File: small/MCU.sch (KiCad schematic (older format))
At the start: 27 parts, among them IC1 PIC32MX350F256H-V_PT, J3 Micro_SD_Card, J4 Conn_01x05_Female, U5 AT25M02, U8 PCF8563T, Y2 Crystal

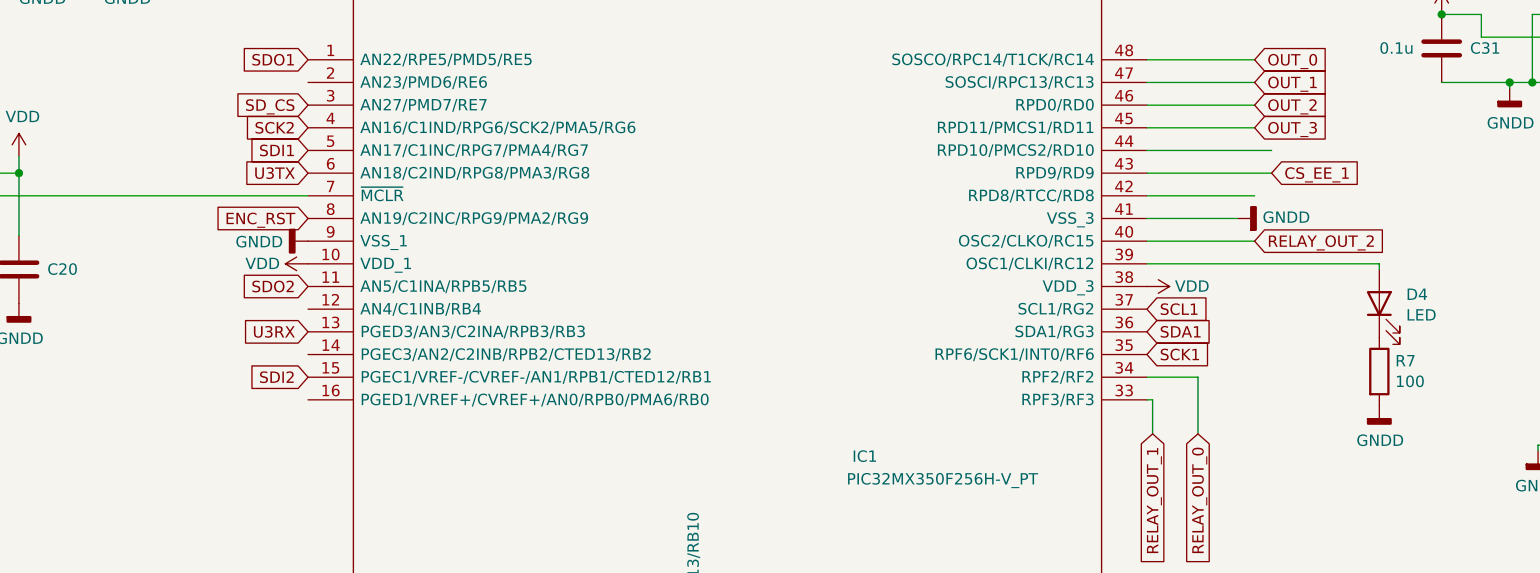
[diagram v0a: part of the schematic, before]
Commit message: sim800 changed to sim808
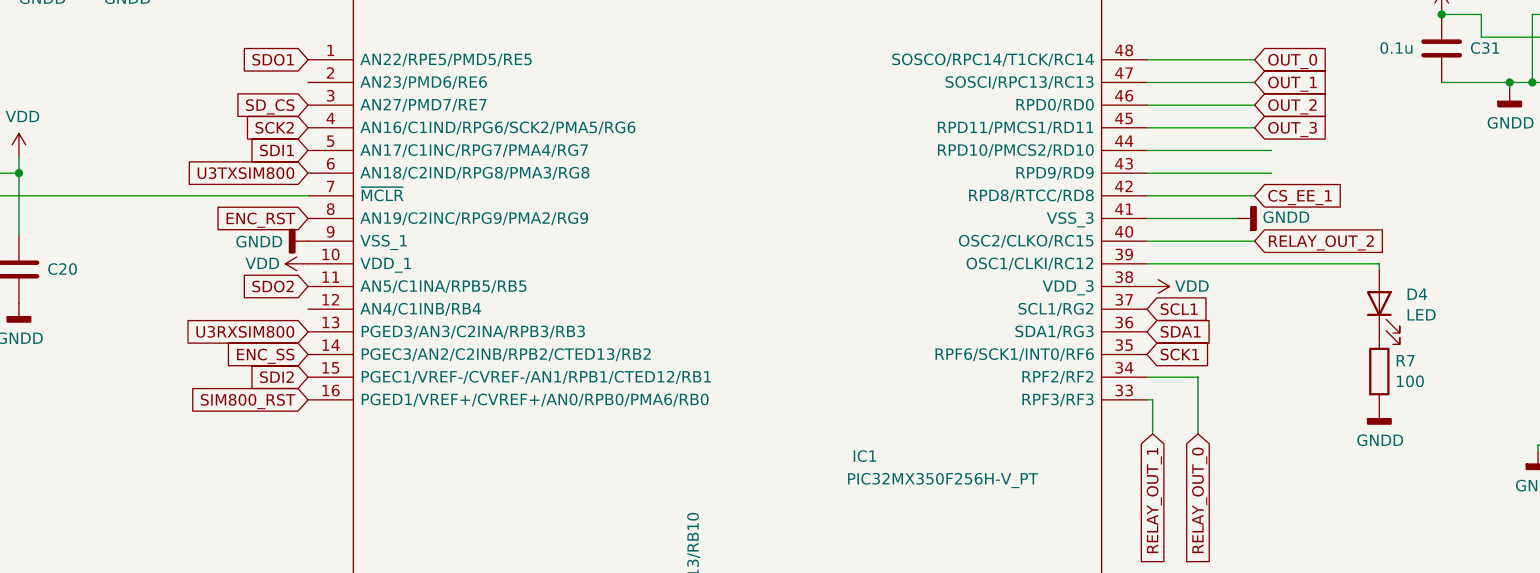
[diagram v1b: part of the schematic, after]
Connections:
- net labels added: ENC_SS, SIM800_RST, U3RXSIM800, U3TXSIM800
- net labels removed: U3RX, U3TX
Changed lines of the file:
@@
 $Descr A4 11693 8268
 encoding utf-8
-Sheet 7 8
+Sheet 7 9
 Title ""
 Date ""
@@
 SCK1
 Text GLabel 3400 4050 0    50   Input ~ 0
-U3RX
+U3RXSIM800
 Wire Wire Line
 	4500 7475 4500 6850
@@
 SD_CS
 Text GLabel 3400 3350 0    50   Input ~ 0
-U3TX
+U3TXSIM800
 Text GLabel 3400 3250 0    50   Input ~ 0
 SDI1
@@
 	1    0    0    -1
 $EndComp
-Text GLabel 7650 3350 2    50   Input ~ 0
+Text GLabel 7575 3450 2    50   Input ~ 0
 CS_EE_1
 $Comp
@@
 Wire Wire Line
 	8250 1150 7900 1150
+Text GLabel 3400 4350 0    50   Input ~ 0
+SIM800_RST
+Text GLabel 3400 4150 0    50   Input ~ 0
+ENC_SS
 $EndSCHEMATC

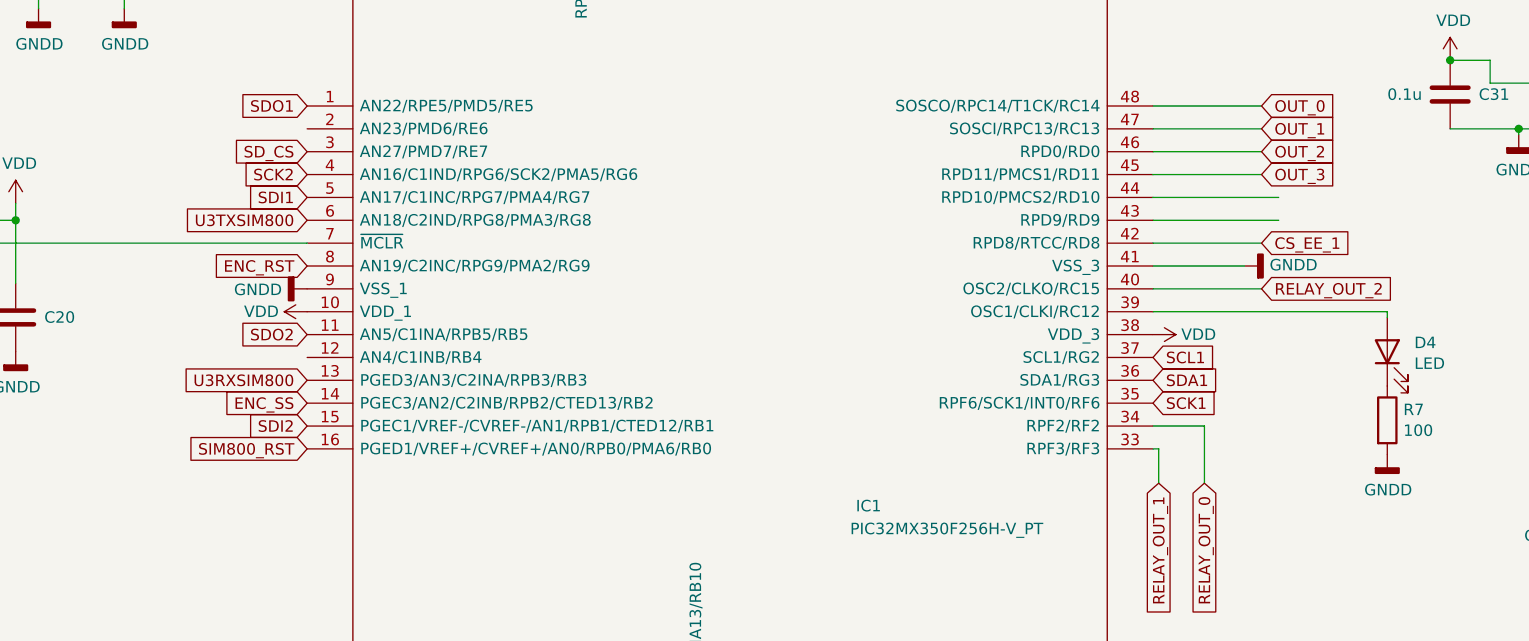
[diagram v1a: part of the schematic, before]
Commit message: All routed PGEC1 grounded according to errata
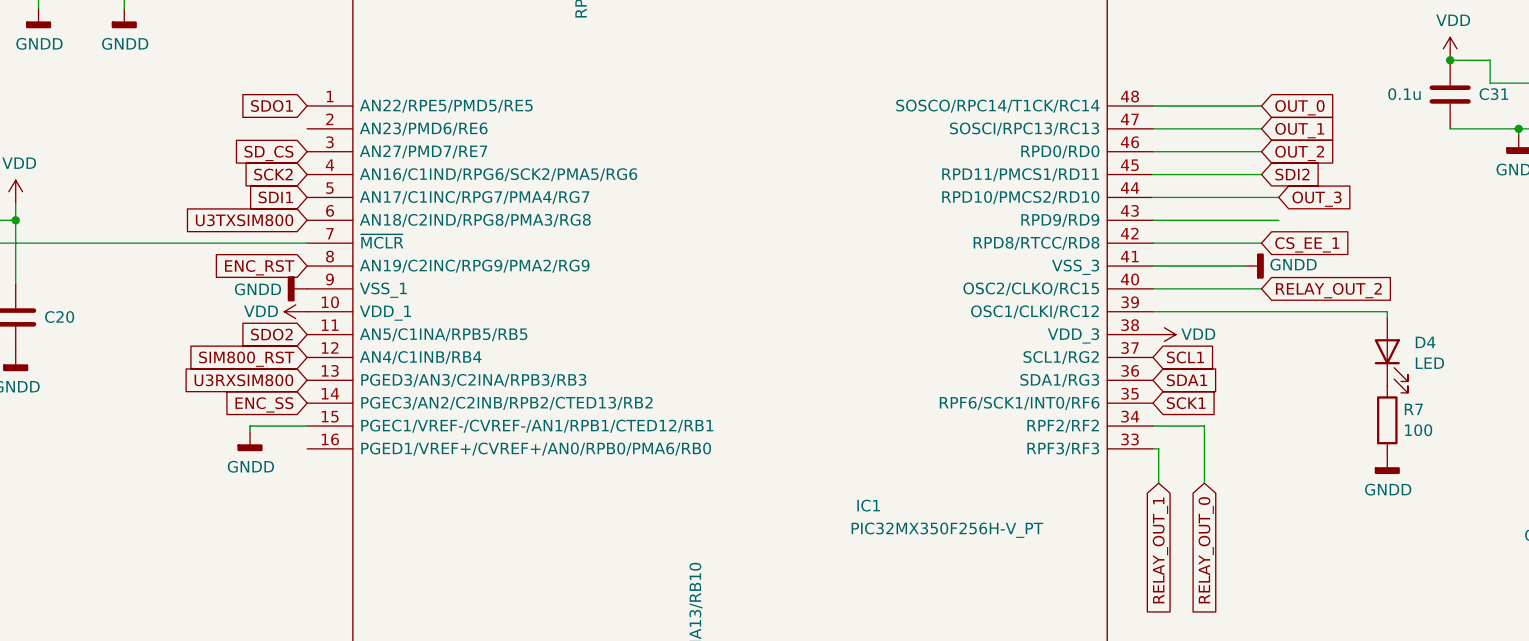
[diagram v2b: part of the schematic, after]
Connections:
- wire segments 98 -> 100
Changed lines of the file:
@@
 Wire Wire Line
 	5300 725  5300 1450
-Text GLabel 3400 4250 0    50   Input ~ 0
-SDI2
 Text GLabel 3400 3850 0    50   Input ~ 0
 SDO2
@@
 Text GLabel 7575 3050 2    50   Input ~ 0
 OUT_2
-Text GLabel 7575 3150 2    50   Input ~ 0
-OUT_3
 Wire Wire Line
 	8800 2950 8800 2650
@@
 Wire Wire Line
 	8250 1150 7900 1150
-Text GLabel 3400 4350 0    50   Input ~ 0
+Text GLabel 3400 3950 0    50   Input ~ 0
 SIM800_RST
 Text GLabel 3400 4150 0    50   Input ~ 0
 ENC_SS
+Text GLabel 7650 3250 2    50   Input ~ 0
+OUT_3
+Text GLabel 7575 3150 2    50   Input ~ 0
+SDI2
+$Comp
+L power:GNDD #PWR?
+U 1 1 606D287A
+P 3150 4275
+F 0 "#PWR?" H 3150 4025 50  0001 C CNN
+F 1 "GNDD" H 3154 4120 50  0000 C CNN
+F 2 "" H 3150 4275 50  0001 C CNN
+F 3 "" H 3150 4275 50  0001 C CNN
+	1    3150 4275
+	1    0    0    -1
+$EndComp
+Wire Wire Line
+	3400 4250 3150 4250
+Wire Wire Line
+	3150 4250 3150 4275
 $EndSCHEMATC

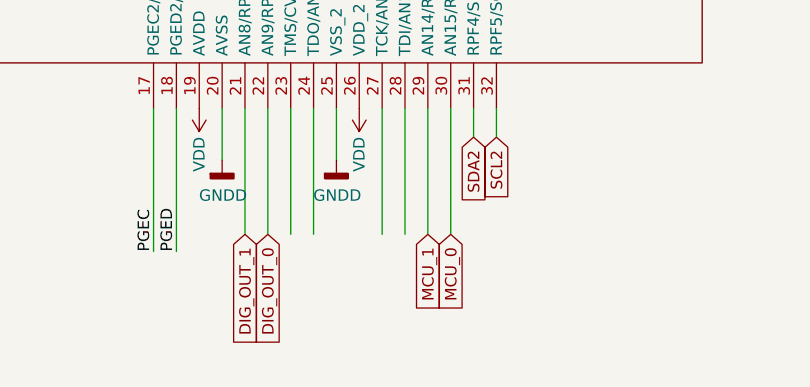
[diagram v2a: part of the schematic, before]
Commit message: connector rotated.
added rs485 output.

TODO: add bluetooth port.
check all parts
preaper bom list
prepare mouser list
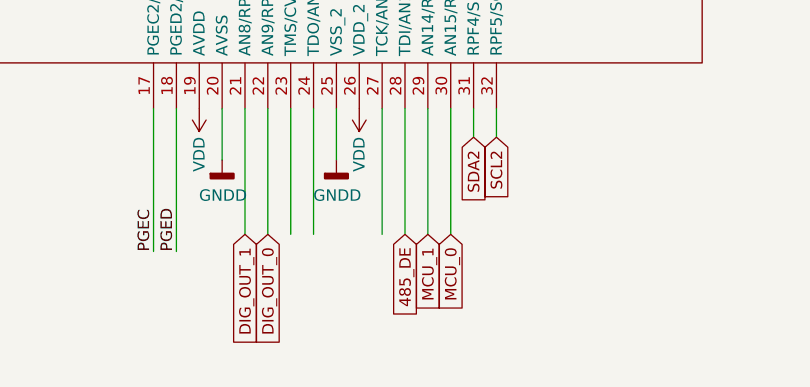
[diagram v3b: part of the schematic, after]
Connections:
- net labels added: 485_DE
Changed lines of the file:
@@
 SDI2
 $Comp
-L power:GNDD #PWR?
+L power:GNDD #PWR0184
 U 1 1 606D287A
 P 3150 4275
-F 0 "#PWR?" H 3150 4025 50  0001 C CNN
+F 0 "#PWR0184" H 3150 4025 50  0001 C CNN
 F 1 "GNDD" H 3154 4120 50  0000 C CNN
 F 2 "" H 3150 4275 50  0001 C CNN
@@
 Wire Wire Line
 	3150 4250 3150 4275
+Text GLabel 5600 7400 3    50   Input ~ 0
+485_DE
 $EndSCHEMATC

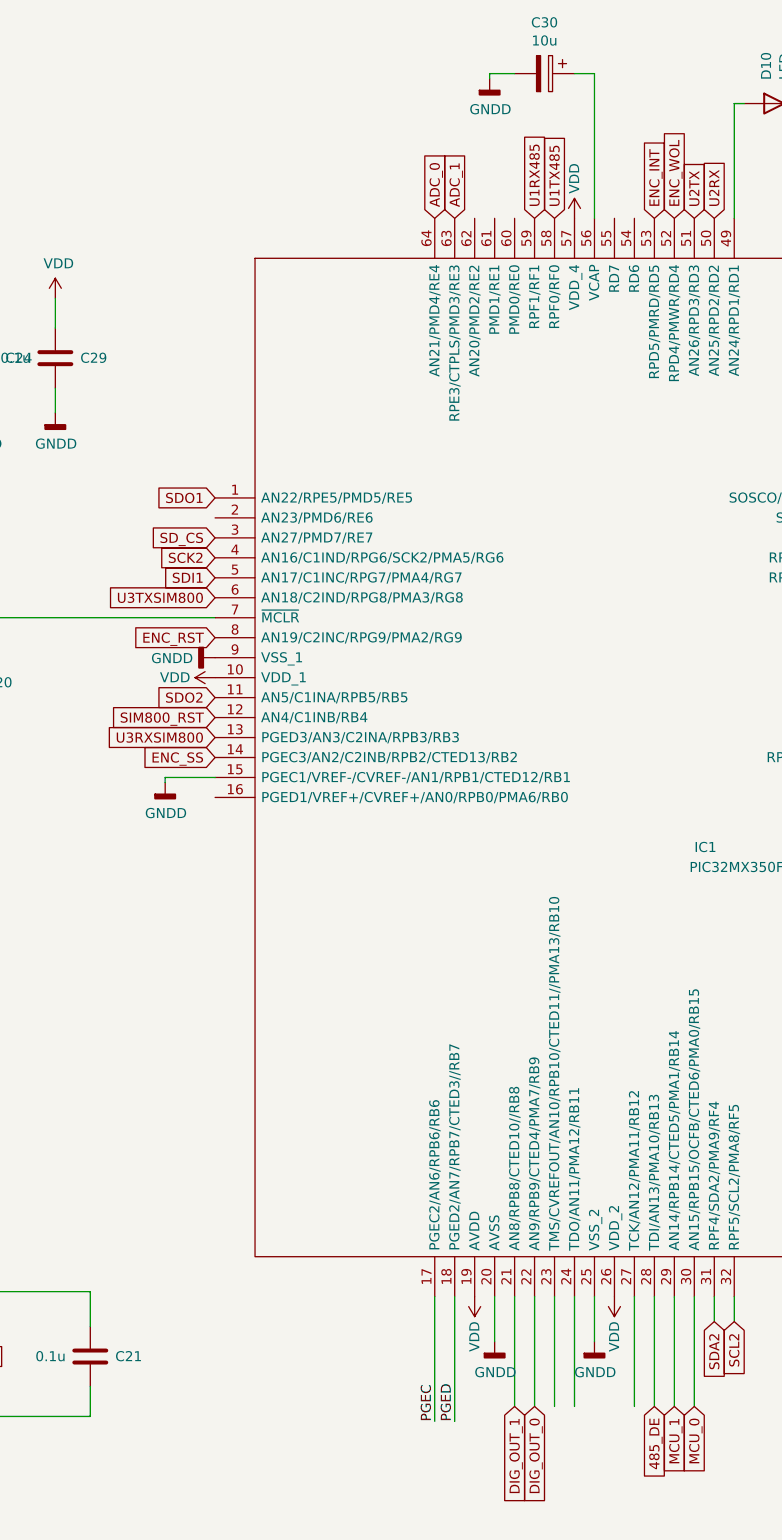
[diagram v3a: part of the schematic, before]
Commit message: GPS connector moved,
antenna matching networks removed

SUPERCAPACITOR from jlpcb used.
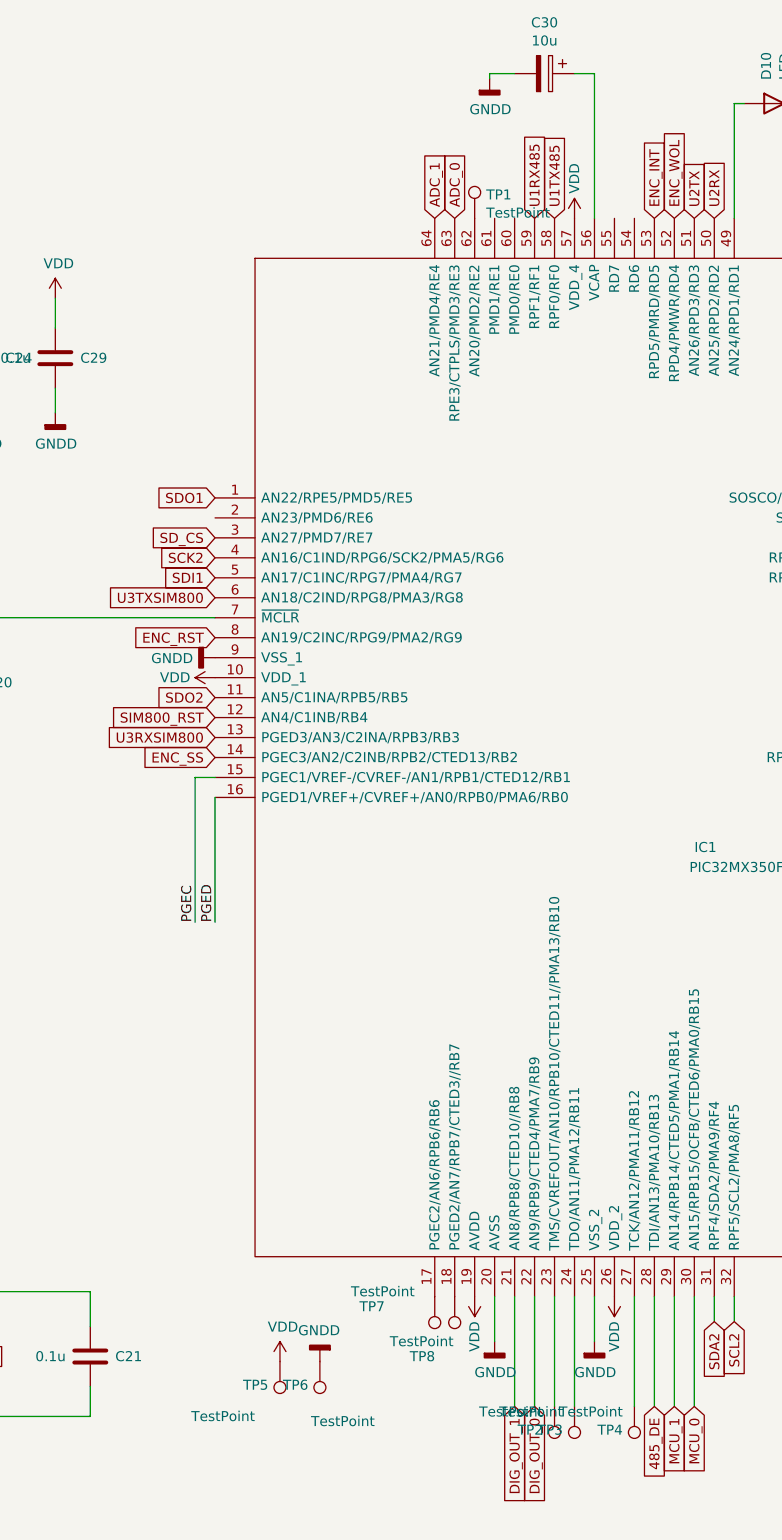
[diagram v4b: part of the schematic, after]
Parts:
- added TP1, TP2, TP3, TP4, TP5, TP6, TP7, TP8: TestPoint, TestPoint:TestPoint_Pad_1.5x1.5mm, symbol Connector:TestPoint
- C25: footprint Capacitor_THT:C_Disc_D11.0mm_W5.0mm_P5.00mm -> small:XH414HG-IV01E; LCSC (none) -> C38065
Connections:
- wire segments 100 -> 99
